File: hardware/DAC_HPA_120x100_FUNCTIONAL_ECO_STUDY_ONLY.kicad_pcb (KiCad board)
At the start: 4 copper layers, 120 x 100 mm, 544 parts, among them J101 GCT USB4105-GF-A, J201 PCB pads (no component), J202 PCB pads (no component), J701 G-Switch GT-3321667P-01, J702 HRO PJ-332A-6A, K601 TLP3545A, K602 TLP3545A, K603 TLP3545A, K604 TLP3545A, Q207 AO3400A, Q502 AO3400A, Q503 AO3400A, Q504 AO3400A, Q505 AO3400A, Q506 AO3400A, Q507 MMBT3904, Q612 MMBT3904, Q614 MMBT3904, Q616 AO3400A, Q617 AO3400A, Q618 2N7002, Q619 AO3400A, Q620 AO3400A, Q621 2N7002, Q622 AO3400A, Q623 MMBT3904, Q624 MMBT3904, Q625 MMBT3904, Q626 MMBT3904, Q627 MMBT3904, U101 ST USBLC6-2SC6, U102 TI TPS25200DRVR, U103 TI TPD2E2U06DRLR, U201 CH32V307RCT6, U202 AGRV2KQ32, U205 74LVC1G157, U206 74LVC1G11, U208 74LVC3G34, U301 ES9018K2M, U302 3.3 V, 250 mA, U303 1.300 V (R533/R534), U401 OPA1622IDRCR, U402 OPA1622IDRCR, U403 OPA2210IDGKR, U404 OPA2210IDGKR, U501 +3.85 / -3.72 V, U502 3.3 V, 150 mA, U503 TI TPS259621DDAR, U504 3.3 V, 1 A, U505 TI TMUX1101DBVR, U603 TLV1704, U604 OPA2333, U605 TLV3402, U606 TLV1704, U607 74AUP1G17, U608 74LVC1G74, U609 TLV1704, U610 TLV1704, U611 TLV1704, U612 TLV1704, U613 TLV3402, U614 TLV3402, U615 TLV3402, U616 TLV3402, U617 TLV3402, U618 TLV3402, U619 TLV3402, U620 TLV3402, U621 SN74AUP2G17DCKR, X201 80.000 MHz, X202 49.152 MHz, X203 45.1584 MHz, Y201 8 MHz

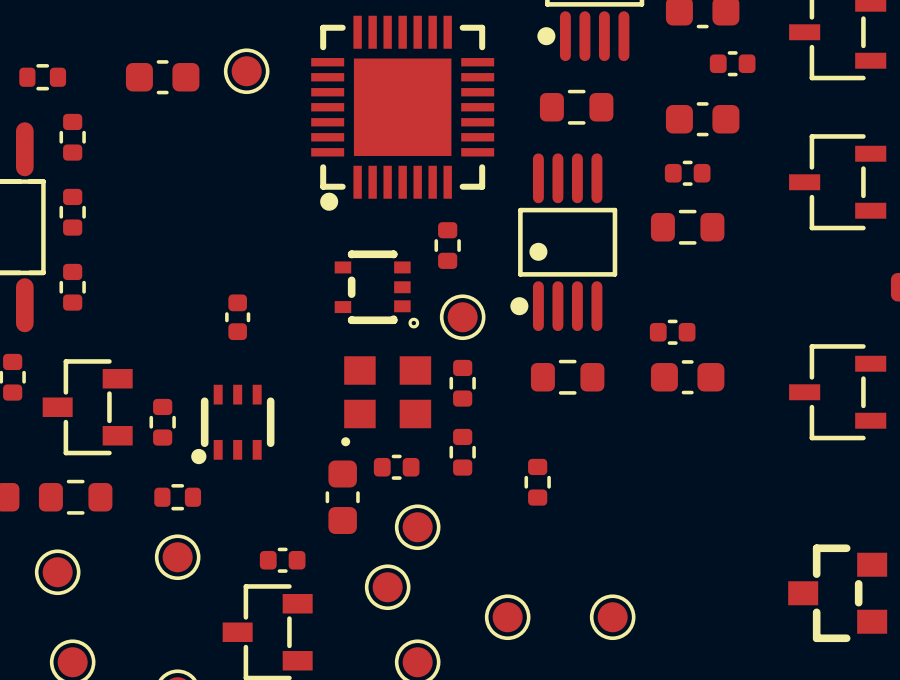
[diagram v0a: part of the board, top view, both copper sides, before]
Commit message: Hand-route 80 MHz clock and ground pull-down on ECO board
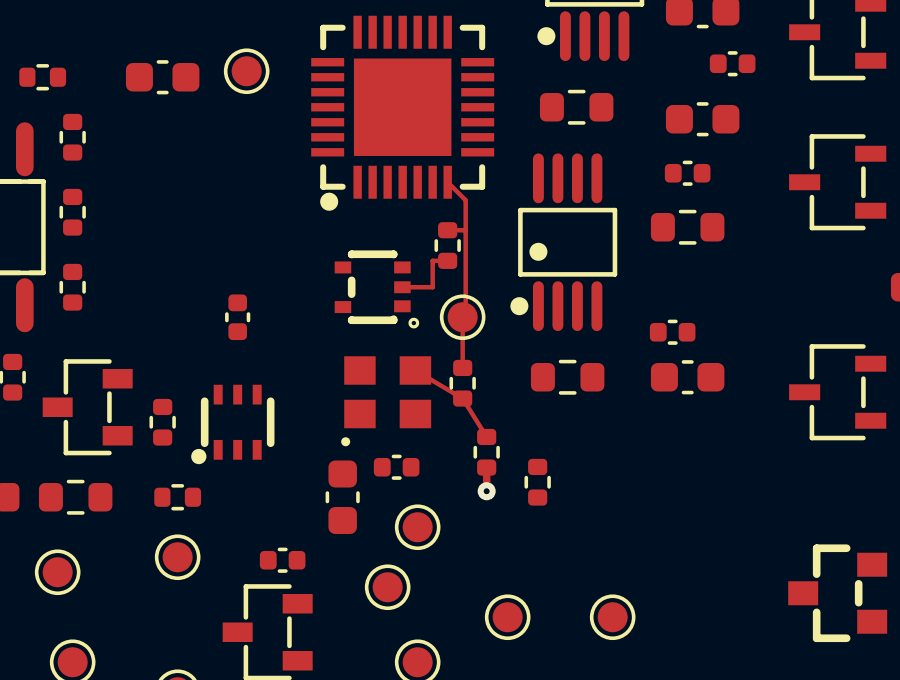
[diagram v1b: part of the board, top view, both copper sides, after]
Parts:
- moved R227 0.80 mm to (93.3, 92.5), turned to -90 degrees
- turned R203 to 90 degrees
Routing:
- net MCLK: track 0.00 -> 7.08 mm
- net N2_X201_OUT: track 0.00 -> 3.34 mm
- net N6_MCK_IN: track 0.00 -> 2.39 mm
- net GND: track 6.28 -> 7.07 mm, vias 6 -> 7
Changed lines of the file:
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@@
 				(font
 					(size 1.27 1.27)
+					(thickness 0.15)
 				)
 			)
@@
 				(font
 					(size 1.27 1.27)
+					(thickness 0.15)
 				)
 			)
@@
 	(footprint "Resistor_SMD:R_0402_1005Metric"
 		(layer "F.Cu")
-		(at 92.5 92.5 90)
+		(at 93.3 92.5 -90)
 		(descr "Resistor SMD 0402 (1005 Metric), square (rectangular) end terminal, IPC-7351 nominal, (Body size source: IPC-SM-782 page 72, https://www.pcb-3d.com/wordpress/wp-content/uploads/ipc-sm-782a_amendment_1_and_2.pdf)")
 		(tags "resistor")
 		(property "Reference" "R227"
-			(at 0 -1.17 90)
+			(at 0 -1.17 270)
 			(layer "F.Fab")
 			(effects
@@
 		)
 		(property "Value" "10 kΩ"
-			(at 0 1.17 90)
+			(at 0 1.17 270)
 			(layer "F.Fab")
 			(hide yes)
@@
 		)
 		(property "Datasheet" ""
-			(at 0 0 90)
+			(at 0 0 270)
 			(layer "F.Fab")
 			(hide yes)
@@
 		)
 		(property "Description" ""
-			(at 0 0 90)
+			(at 0 0 270)
 			(layer "F.Fab")
 			(hide yes)
@@
 		)
 		(property "KiLib_Generator" "SMD_2terminal_chip_molded"
-			(at 0 0 90)
+			(at 0 0 270)
 			(layer "F.SilkS")
 			(hide yes)
@@
 		(duplicate_pad_numbers_are_jumpers no)
 		(fp_line
-			(start -0.153641 -0.38)
-			(end 0.153641 -0.38)
+			(start -0.153641 0.38)
+			(end 0.153641 0.38)
 			(stroke
 				(width 0.12)
@@
 		)
 		(fp_line
-			(start -0.153641 0.38)
-			(end 0.153641 0.38)
+			(start -0.153641 -0.38)
+			(end 0.153641 -0.38)
 			(stroke
 				(width 0.12)
@@
 		)
 		(fp_text user "${REFERENCE}"
-			(at 0 0 90)
+			(at 0 0 270)
 			(layer "F.Fab")
 			(effects
@@
 		)
 		(pad "1" smd roundrect
-			(at -0.51 0 90)
+			(at -0.51 0 270)
 			(size 0.54 0.64)
 			(layers "F.Cu" "F.Mask" "F.Paste")
@@
 		)
 		(pad "2" smd roundrect
-			(at 0.51 0 90)
+			(at 0.51 0 270)
 			(size 0.54 0.64)
 			(layers "F.Cu" "F.Mask" "F.Paste")
@@
 				(font
 					(size 1.27 1.27)
+					(thickness 0.15)
 				)
 			)
@@
 				(font
 					(size 1.27 1.27)
+					(thickness 0.15)
 				)
 			)
@@
 				(font
 					(size 1.27 1.27)
+					(thickness 0.15)
 				)
 			)
@@
 				(font
 					(size 1.27 1.27)
+					(thickness 0.15)
 				)
 			)
@@
 	(footprint "Resistor_SMD:R_0402_1005Metric"
 		(layer "F.Cu")
-		(at 92.5 90.2 -90)
+		(at 92.5 90.2 90)
 		(descr "Resistor SMD 0402 (1005 Metric), square (rectangular) end terminal, IPC-7351 nominal, (Body size source: IPC-SM-782 page 72, https://www.pcb-3d.com/wordpress/wp-content/uploads/ipc-sm-782a_amendment_1_and_2.pdf)")
 		(tags "resistor")
 		(property "Reference" "R203"
-			(at 0 -1.17 270)
+			(at 0 -1.17 90)
 			(layer "F.Fab")
 			(effects
@@
 		)
 		(property "Value" "33 Ω"
-			(at 0 1.17 270)
+			(at 0 1.17 90)
 			(layer "F.Fab")
 			(hide yes)
@@
 		)
 		(property "Datasheet" ""
-			(at 0 0 270)
+			(at 0 0 90)
 			(layer "F.Fab")
 			(hide yes)
@@
 		)
 		(property "Description" ""
-			(at 0 0 270)
+			(at 0 0 90)
 			(layer "F.Fab")
 			(hide yes)
@@
 		)
 		(property "KiLib_Generator" "SMD_2terminal_chip_molded"
-			(at 0 0 270)
+			(at 0 0 90)
 			(layer "F.SilkS")
 			(hide yes)
@@
 		(duplicate_pad_numbers_are_jumpers no)
 		(fp_line
-			(start -0.153641 0.38)
-			(end 0.153641 0.38)
+			(start -0.153641 -0.38)
+			(end 0.153641 -0.38)
 			(stroke
 				(width 0.12)
@@
 		)
 		(fp_line
-			(start -0.153641 -0.38)
-			(end 0.153641 -0.38)
+			(start -0.153641 0.38)
+			(end 0.153641 0.38)
 			(stroke
 				(width 0.12)
@@
 		)
 		(fp_text user "${REFERENCE}"
-			(at 0 0 270)
+			(at 0 0 90)
 			(layer "F.Fab")
 			(effects
@@
 		)
 		(pad "1" smd roundrect
-			(at -0.51 0 270)
+			(at -0.51 0 90)
 			(size 0.54 0.64)
 			(layers "F.Cu" "F.Mask" "F.Paste")
@@
 		)
 		(pad "2" smd roundrect
-			(at 0.51 0 270)
+			(at 0.51 0 90)
 			(size 0.54 0.64)
 			(layers "F.Cu" "F.Mask" "F.Paste")
@@
 	)
 	(segment
+		(start 93.3 93.01)
+		(end 93.3 93.8)
+		(width 0.25)
+		(layer "F.Cu")
+		(net "GND")
+	)
+	(segment
 		(start 151.25 102.3)
 		(end 150.2 102.3)
@@
 		(net "GND")
 	)
-	(segment
-		(start 148.31 113.1)
-		(end 148.31 116.35)
-		(width 0.5)
-		(layer "F.Cu")
-		(net "JACK_LP")
-	)
-	(segment
-		(start 139.6 83.28)
-		(end 139.55 79.45)
-		(width 0.5)
-		(layer "F.Cu")
-		(net "JACK_LP")
+	(via
+		(at 93.3 93.8)
+		(size 0.6)
+		(drill 0.2)
+		(layers "F.Cu" "B.Cu")
+		(net "GND")
 	)
 	(segment
@@
 	)
 	(segment
+		(start 148.31 113.1)
+		(end 148.31 116.35)
+		(width 0.5)
+		(layer "F.Cu")
+		(net "JACK_LP")
+	)
+	(segment
+		(start 139.6 83.28)
+		(end 139.55 79.45)
+		(width 0.5)
+		(layer "F.Cu")
+		(net "JACK_LP")
+	)
+	(segment
+		(start 90.925 89.775)
+		(end 92.5 90.71)
+		(width 0.15)
+		(layer "F.Cu")
+		(net "N2_X201_OUT")
+	)
+	(segment
+		(start 92.5 90.71)
+		(end 93.3 91.99)
+		(width 0.15)
+		(layer "F.Cu")
+		(net "N2_X201_OUT")
+	)
+	(segment
 		(start 147.55 68.72)
 		(end 147.55 72.75)
@@
 		(net "JACK_RN")
 	)
+	(segment
+		(start 92.6 85.1)
+		(end 92.6 84.1)
+		(width 0.15)
+		(layer "F.Cu")
+		(net "MCLK")
+	)
+	(segment
+		(start 92.6 87.9)
+		(end 92.6 85.1)
+		(width 0.15)
+		(layer "F.Cu")
+		(net "MCLK")
+	)
+	(segment
+		(start 92.6 84.1)
+		(end 92.001 83.5)
+		(width 0.15)
+		(layer "F.Cu")
+		(net "MCLK")
+	)
+	(segment
+		(start 92.5 88)
+		(end 92.6 87.9)
+		(width 0.15)
+		(layer "F.Cu")
+		(net "MCLK")
+	)
+	(segment
+		(start 92.6 85.1)
+		(end 92 85.1)
+		(width 0.15)
+		(layer "F.Cu")
+		(net "MCLK")
+	)
+	(segment
+		(start 92.5 89.69)
+		(end 92.5 88)
+		(width 0.15)
+		(layer "F.Cu")
+		(net "MCLK")
+	)
+	(segment
+		(start 91.5 86.12)
+		(end 91.5 87)
+		(width 0.15)
+		(layer "F.Cu")
+		(net "N6_MCK_IN")
+	)
+	(segment
+		(start 92 86.12)
+		(end 91.5 86.12)
+		(width 0.15)
+		(layer "F.Cu")
+		(net "N6_MCK_IN")
+	)
+	(segment
+		(start 91.5 87)
+		(end 90.49 87)
+		(width 0.15)
+		(layer "F.Cu")
+		(net "N6_MCK_IN")
+	)
 	(zone
